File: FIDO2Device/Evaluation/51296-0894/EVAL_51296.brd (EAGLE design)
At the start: 25 x 30 mm, 14 parts, among them CN1 51296-0894, CN2 IF_6PIN, CN3 IF_4PIN, Q1 BSS84AKQBZ, U1 RV-3028-C7

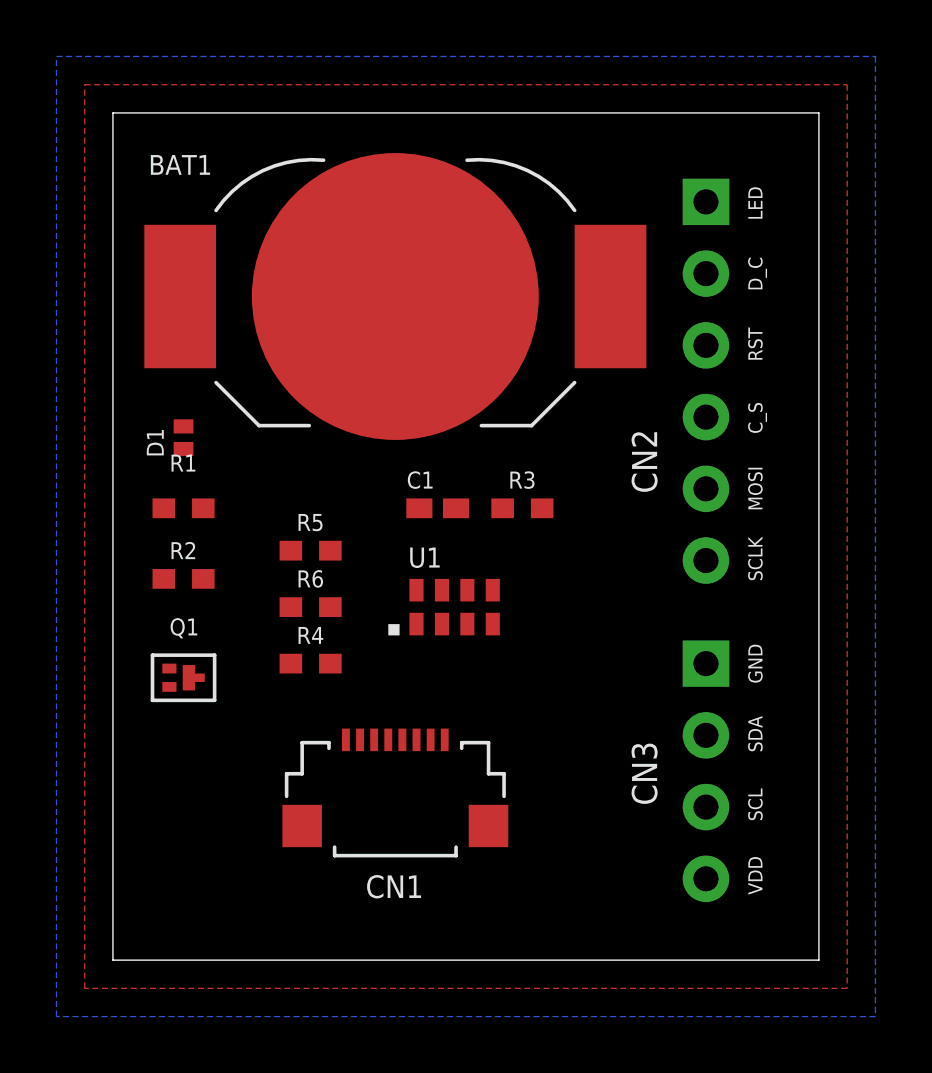
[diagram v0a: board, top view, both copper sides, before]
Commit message: 配線レイアウトを作成
・部品の配置を変更
（RTCC回路を基板の右下部に寄せる）
・電源ライン用のviaを配置
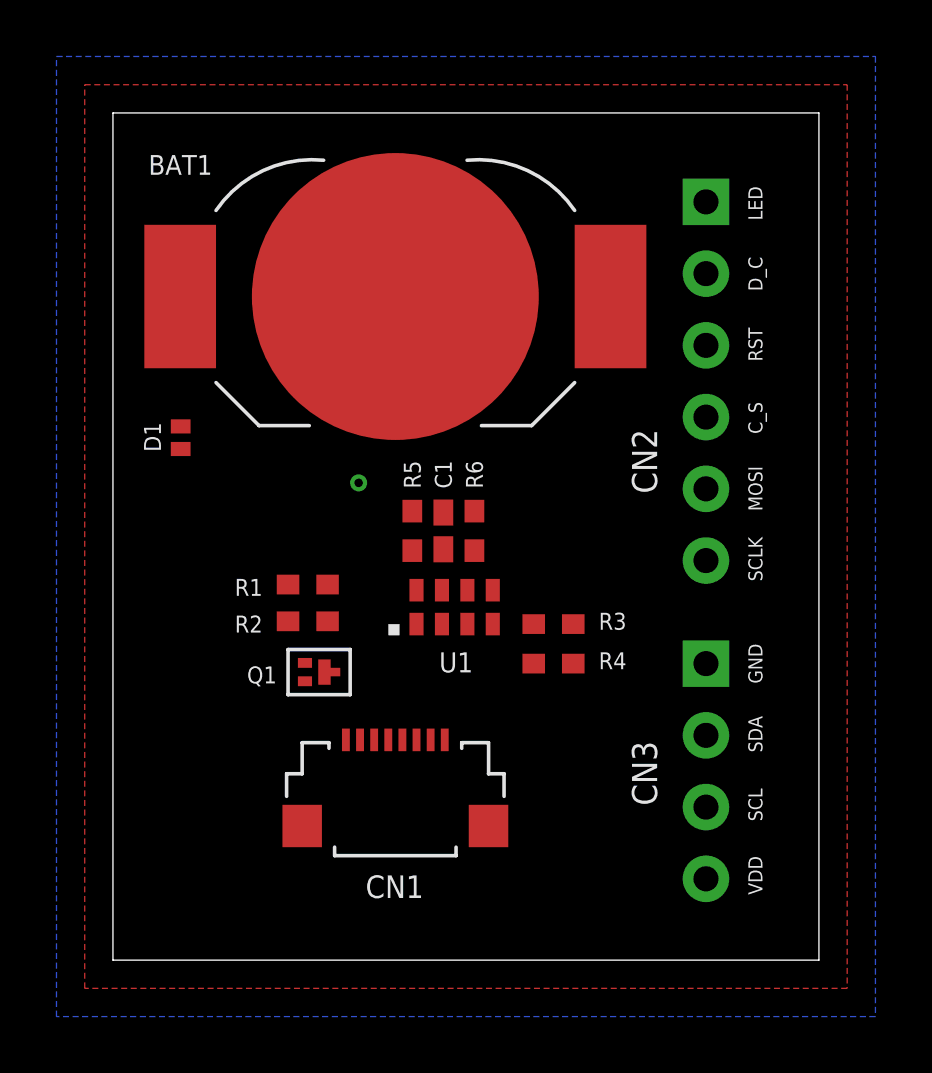
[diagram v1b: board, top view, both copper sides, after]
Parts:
- moved R4 8.60 mm to (15.6, 10.5)
- moved R6 6.40 mm to (12.8, 15.2), turned to 270 degrees
- moved R1 5.16 mm to (6.90, 13.3)
- moved Q1 4.80 mm to (7.30, 10.2)
- moved R2 4.65 mm to (6.90, 12.0)
- moved R3 4.24 mm to (15.6, 11.9)
- moved R5 3.67 mm to (10.6, 15.2), turned to 270 degrees
- moved C1 0.82 mm to (11.7, 15.2), turned to 90 degrees
- moved D1 0.10 mm to (2.40, 18.5)
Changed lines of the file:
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@@
 <attribute name="VALUE" x="19.73" y="11.77" size="0.889" layer="27" ratio="11" rot="R270" align="top-left"/>
 </element>
-<element name="Q1" library="Parts" package="BSS84AKQB" value="BSS84AKQBZ" x="2.5" y="10" smashed="yes" rot="R90">
-<attribute name="NAME" x="2" y="11.5" size="0.6" layer="25"/>
-<attribute name="VALUE" x="2.5" y="11" size="0.6" layer="27" rot="R90"/>
+<element name="Q1" library="Parts" package="BSS84AKQB" value="BSS84AKQBZ" x="7.3" y="10.2" smashed="yes" rot="R90">
+<attribute name="NAME" x="5.8" y="10.4" size="0.6" layer="25" rot="R180"/>
+<attribute name="VALUE" x="7.3" y="11.2" size="0.6" layer="27" rot="R90"/>
 </element>
 <element name="BAT1" library="Connectors" package="BAT-HLD-012-SMT" value="BAT-HLD-012-SMT" x="10" y="23.5" smashed="yes" rot="R180">
@@
 <attribute name="VALUE" x="0.17" y="22.71" size="0.7" layer="27" rot="R180"/>
 </element>
-<element name="R1" library="Parts" package="R0402N" value="5.1k" x="2.5" y="16" smashed="yes" rot="R180">
-<attribute name="NAME" x="2" y="17.3" size="0.6" layer="25"/>
-<attribute name="VALUE" x="3" y="17.3" size="0.6" layer="27" rot="R180"/>
+<element name="R1" library="Parts" package="R0402N" value="5.1k" x="6.9" y="13.3" smashed="yes" rot="R180">
+<attribute name="NAME" x="5.3" y="13.5" size="0.6" layer="25" rot="R180"/>
+<attribute name="VALUE" x="7.4" y="14.6" size="0.6" layer="27" rot="R180"/>
 </element>
-<element name="R2" library="Parts" package="R0402N" value="20k" x="2.5" y="13.5" smashed="yes">
-<attribute name="NAME" x="2" y="14.2" size="0.6" layer="25"/>
-<attribute name="VALUE" x="2" y="12.2" size="0.6" layer="27"/>
+<element name="R2" library="Parts" package="R0402N" value="20k" x="6.9" y="12" smashed="yes">
+<attribute name="NAME" x="5.3" y="12.2" size="0.6" layer="25" rot="R180"/>
+<attribute name="VALUE" x="6.4" y="10.7" size="0.6" layer="27"/>
 </element>
-<element name="U1" library="ICs" package="SON-8" value="RV-3028-C7" x="10.5" y="11.5"/>
-<element name="R3" library="Parts" package="R0402N" value="10k" x="14.5" y="16"/>
-<element name="R4" library="Parts" package="R0402N" value="10k" x="7" y="10.5"/>
-<element name="R5" library="Parts" package="R0402N" value="10k" x="7" y="14.5" smashed="yes">
-<attribute name="NAME" x="6.5" y="15.2" size="0.6" layer="25"/>
-<attribute name="VALUE" x="6.5" y="13.2" size="0.6" layer="27"/>
+<element name="U1" library="ICs" package="SON-8" value="RV-3028-C7" x="10.5" y="11.5" smashed="yes">
+<attribute name="NAME" x="12.75" y="10.9" size="0.7112" layer="25" rot="R180"/>
+<attribute name="VALUE" x="10.45" y="10.4" size="0.7112" layer="27"/>
 </element>
-<element name="C1" library="Parts" package="C0402N" value="0.1uF" x="11.5" y="16"/>
-<element name="R6" library="Parts" package="R0402N" value="10k" x="7" y="12.5"/>
-<element name="D1" library="Parts" package="DFN1006D-2" value="PMEG2005BELD,315" x="2.5" y="18.5" rot="R90"/>
+<element name="R3" library="Parts" package="R0402N" value="10k" x="15.6" y="11.9" smashed="yes">
+<attribute name="NAME" x="17.2" y="11.7" size="0.6" layer="25"/>
+<attribute name="VALUE" x="15.1" y="10.6" size="0.6" layer="27"/>
+</element>
+<element name="R4" library="Parts" package="R0402N" value="10k" x="15.6" y="10.5" smashed="yes">
+<attribute name="NAME" x="17.2" y="10.3" size="0.6" layer="25"/>
+<attribute name="VALUE" x="15.1" y="9.2" size="0.6" layer="27"/>
+</element>
+<element name="R5" library="Parts" package="R0402N" value="10k" x="10.6" y="15.2" smashed="yes" rot="R270">
+<attribute name="NAME" x="10.9" y="16.7" size="0.6" layer="25" rot="R90"/>
+<attribute name="VALUE" x="9.3" y="15.7" size="0.6" layer="27" rot="R270"/>
+</element>
+<element name="C1" library="Parts" package="C0402N" value="0.1uF" x="11.7" y="15.2" smashed="yes" rot="R90">
+<attribute name="NAME" x="12" y="16.7" size="0.6" layer="25" rot="R90"/>
+<attribute name="VALUE" x="13" y="14.1" size="0.6" layer="27" rot="R90"/>
+</element>
+<element name="R6" library="Parts" package="R0402N" value="10k" x="12.8" y="15.2" smashed="yes" rot="R270">
+<attribute name="NAME" x="13.1" y="16.7" size="0.6" layer="25" rot="R90"/>
+<attribute name="VALUE" x="11.5" y="15.7" size="0.6" layer="27" rot="R270"/>
+</element>
+<element name="D1" library="Parts" package="DFN1006D-2" value="PMEG2005BELD,315" x="2.4" y="18.5" smashed="yes" rot="R90">
+<attribute name="NAME" x="1.7" y="18" size="0.6" layer="25" rot="R90"/>
+<attribute name="VALUE" x="3.1" y="17.8" size="0.6" layer="27" rot="R90" align="top-left"/>
+</element>
 </elements>
 <signals>
@@
 <contactref element="CN1" pad="1"/>
 <contactref element="Q1" pad="3"/>
-<wire x1="2.69" y1="10" x2="8.25" y2="7.8" width="0" layer="19" extent="1-1"/>
+<wire x1="7.49" y1="10.2" x2="8.25" y2="7.8" width="0" layer="19" extent="1-1"/>
 </signal>
 <signal name="0V">
@@
 <contactref element="Q1" pad="1"/>
 <contactref element="R2" pad="1"/>
-<wire x1="1.8" y1="13.5" x2="1.8" y2="16" width="0" layer="19" extent="1-1"/>
-<wire x1="2" y1="9.675" x2="1.8" y2="13.5" width="0" layer="19" extent="1-1"/>
+<wire x1="6.2" y1="12" x2="6.2" y2="13.3" width="0" layer="19" extent="1-1"/>
+<wire x1="6.8" y1="9.875" x2="6.2" y2="12" width="0" layer="19" extent="1-1"/>
 </signal>
 <signal name="VDD_NRF">
@@
 <contactref element="R4" pad="2"/>
 <contactref element="D1" pad="1"/>
-<wire x1="15.2" y1="16" x2="21" y2="2.88" width="0" layer="19" extent="1-1"/>
-<wire x1="10.85" y1="16" x2="15.2" y2="16" width="0" layer="19" extent="1-1"/>
-<wire x1="11.65" y1="13.1" x2="10.85" y2="16" width="0" layer="19" extent="1-1"/>
-<wire x1="7.7" y1="10.5" x2="11.65" y2="13.1" width="0" layer="19" extent="1-1"/>
-<wire x1="3.2" y1="13.5" x2="7.7" y2="10.5" width="0" layer="19" extent="1-1"/>
-<wire x1="2" y1="10.325" x2="3.2" y2="13.5" width="0" layer="19" extent="1-1"/>
-<wire x1="11.25" y1="7.8" x2="11.65" y2="13.1" width="0" layer="19" extent="1-1"/>
-<wire x1="2.5" y1="18.1" x2="3.2" y2="13.5" width="0" layer="19" extent="1-1"/>
+<wire x1="16.3" y1="10.5" x2="16.3" y2="11.9" width="0" layer="19" extent="1-1"/>
+<wire x1="11.65" y1="13.1" x2="16.3" y2="11.9" width="0" layer="19" extent="1-1"/>
+<wire x1="11.7" y1="14.55" x2="11.65" y2="13.1" width="0" layer="19" extent="1-1"/>
+<wire x1="7.6" y1="12" x2="11.65" y2="13.1" width="0" layer="19" extent="1-1"/>
+<wire x1="6.8" y1="10.525" x2="7.6" y2="12" width="0" layer="19" extent="1-1"/>
+<wire x1="11.25" y1="7.8" x2="6.8" y2="10.525" width="0" layer="19" extent="1-1"/>
+<wire x1="2.4" y1="18.1" x2="7.6" y2="12" width="0" layer="19" extent="1-1"/>
+<wire x1="21" y1="2.88" x2="16.3" y2="10.5" width="0" layer="19" extent="1-1"/>
 </signal>
 <signal name="LED_CTRL">
 <contactref element="R1" pad="1"/>
 <contactref element="CN2" pad="1"/>
-<wire x1="3.2" y1="16" x2="21" y2="26.85" width="0" layer="19" extent="1-1"/>
+<wire x1="7.6" y1="13.3" x2="21" y2="26.85" width="0" layer="19" extent="1-1"/>
 </signal>
 <signal name="CS">
@@
 <contactref element="R3" pad="1"/>
 <contactref element="CN3" pad="2"/>
-<wire x1="13.8" y1="16" x2="21" y2="7.96" width="0" layer="19" extent="1-1"/>
-<wire x1="13.45" y1="11.9" x2="13.8" y2="16" width="0" layer="19" extent="1-1"/>
+<wire x1="14.9" y1="11.9" x2="21" y2="7.96" width="0" layer="19" extent="1-1"/>
+<wire x1="13.45" y1="11.9" x2="14.9" y2="11.9" width="0" layer="19" extent="1-1"/>
 </signal>
 <signal name="TWI_SCL">
@@
 <contactref element="R4" pad="1"/>
 <contactref element="CN3" pad="3"/>
-<wire x1="12.55" y1="11.9" x2="21" y2="5.42" width="0" layer="19" extent="1-1"/>
-<wire x1="6.3" y1="10.5" x2="12.55" y2="11.9" width="0" layer="19" extent="1-1"/>
+<wire x1="14.9" y1="10.5" x2="21" y2="5.42" width="0" layer="19" extent="1-1"/>
+<wire x1="12.55" y1="11.9" x2="14.9" y2="10.5" width="0" layer="19" extent="1-1"/>
 </signal>
 <signal name="N$9">
 <contactref element="U1" pad="6"/>
 <contactref element="R6" pad="2"/>
-<wire x1="7.7" y1="12.5" x2="12.55" y2="13.1" width="0" layer="19" extent="1-1"/>
+<wire x1="12.55" y1="13.1" x2="12.8" y2="14.5" width="0" layer="19" extent="1-1"/>
 </signal>
 <signal name="N$10">
 <contactref element="U1" pad="8"/>
 <contactref element="R5" pad="2"/>
-<wire x1="10.75" y1="13.1" x2="7.7" y2="14.5" width="0" layer="19" extent="1-1"/>
+<wire x1="10.6" y1="14.5" x2="10.75" y2="13.1" width="0" layer="19" extent="1-1"/>
 </signal>
 <signal name="N$2">
 <contactref element="BAT1" pad="+@2"/>
 <contactref element="D1" pad="2"/>
-<wire x1="2.5" y1="18.9" x2="2.38" y2="23.5" width="0" layer="19" extent="1-1"/>
+<wire x1="2.4" y1="18.9" x2="2.38" y2="23.5" width="0" layer="19" extent="1-1"/>
+</signal>
+<signal name="N$3">
+<via x="8.7" y="16.9" extent="1-16" drill="0.3"/>
 </signal>
 </signals>

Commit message: 配線レイアウトを作成
・電源ラインの配線
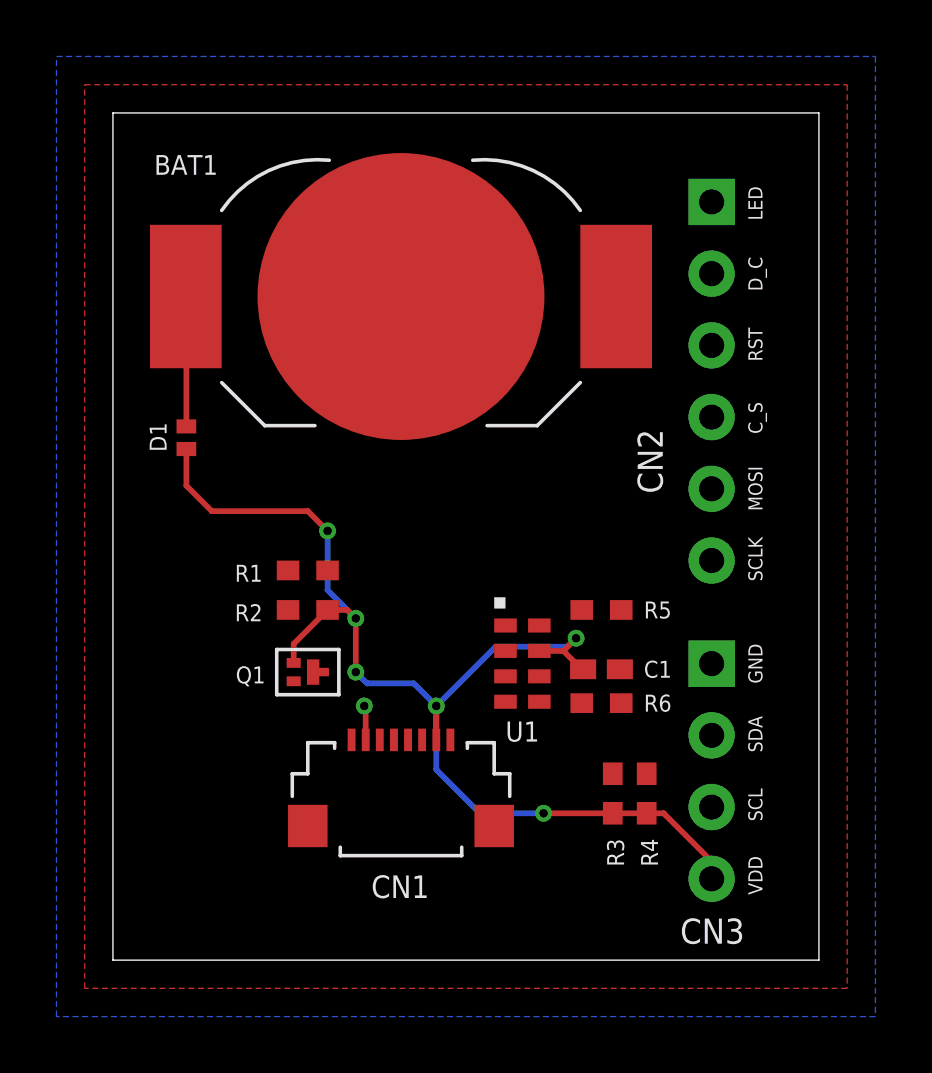
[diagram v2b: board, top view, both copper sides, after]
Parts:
- moved R6 7.58 mm to (17.3, 9.10), turned to 180 degrees
- moved C1 7.44 mm to (17.3, 10.3), turned to 0 degrees
- moved R5 7.26 mm to (17.3, 12.4), turned to 180 degrees
- moved R3 6.36 mm to (17.7, 5.90), turned to 270 degrees
- moved R4 5.66 mm to (18.9, 5.90), turned to 270 degrees
- moved U1 3.06 mm to (13.5, 12.1), turned to 270 degrees
- moved R1 0.50 mm to (6.90, 13.8)
- moved R2 0.40 mm to (6.90, 12.4)
- moved Q1 0.40 mm to (6.90, 10.2)
- moved D1 0.20 mm to (2.60, 18.5)
- moved BAT1 0.20 mm to (10.2, 23.5)
- moved CN1 0.20 mm to (10.2, 4.00)
- moved CN2 0.20 mm to (21.2, 20.5)
- moved CN3 0.20 mm to (21.2, 10.5)
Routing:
- net VDD_NRF: track 0.00 -> 43.0 mm, vias 0 -> 6
- net N$2: track 0.00 -> 4.61 mm
- net 0V: track 0.00 -> 1.22 mm, vias 0 -> 1

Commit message: 配線レイアウトを作成
・LED制御回路、RTCC回路の配線
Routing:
- net LED_CTRL: track 0.00 -> 22.0 mm
- net TWI_SCL: track 0.00 -> 12.7 mm
- net TWI_SDA: track 0.00 -> 9.94 mm
- net N$1: track 0.00 -> 5.18 mm
- net LEDA: track 0.00 -> 3.20 mm
- net N$9: track 0.00 -> 1.89 mm
- net N$10: track 0.00 -> 1.73 mm
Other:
- board text added: "RTCC"
- board text added: "TFT Module"
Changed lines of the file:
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@@
 <dimension x1="0" y1="0" x2="0" y2="30" x3="-3" y3="15" textsize="1.778" layer="51"/>
 <dimension x1="0" y1="30" x2="25" y2="30" x3="12.5" y3="33" textsize="1.778" layer="51"/>
+<text x="23.4" y="20.5" size="0.7" layer="21" rot="R90" align="top-center">TFT Module</text>
+<text x="23.4" y="6.7" size="0.7" layer="21" rot="R90" align="top-center">RTCC</text>
 </plain>
 <attributes>
@@
 </element>
 <element name="CN2" library="Connectors" package="HEADER_6PIN" value="IF_6PIN" x="21.2" y="20.5" smashed="yes" rot="R270">
-<attribute name="NAME" x="19.47" y="16.52" size="0.889" layer="25" ratio="11" rot="R90"/>
+<attribute name="NAME" x="19.97" y="28.32" size="0.889" layer="25" ratio="11"/>
 <attribute name="VALUE" x="19.93" y="28.12" size="0.889" layer="27" ratio="11" rot="R270" align="top-left"/>
 </element>
@@
 <contactref element="CN1" pad="1"/>
 <contactref element="Q1" pad="3"/>
-<wire x1="7.09" y1="10.2" x2="8.45" y2="7.8" width="0" layer="19" extent="1-1"/>
+<wire x1="8.45" y1="7.8" x2="8.45" y2="8.45" width="0.2032" layer="1"/>
+<wire x1="8.45" y1="8.45" x2="7.9" y2="9" width="0.2032" layer="1"/>
+<wire x1="7.9" y1="9" x2="7.5" y2="9" width="0.2032" layer="1"/>
+<wire x1="7.09" y1="10.2" x2="7.09" y2="9.41" width="0.2032" layer="1"/>
+<wire x1="7.09" y1="9.41" x2="7.5" y2="9" width="0.2032" layer="1"/>
 </signal>
 <signal name="0V">
@@
 <vertex x="-2" y="-2"/>
 </polygon>
-<via x="8.9" y="9" extent="1-16" drill="0.3"/>
-<wire x1="8.95" y1="7.8" x2="8.95" y2="8.95" width="0.2032" layer="1"/>
-<wire x1="8.95" y1="8.95" x2="8.9" y2="9" width="0.2032" layer="1"/>
+<via x="8.9" y="6.6" extent="1-16" drill="0.3"/>
+<wire x1="8.95" y1="7.8" x2="8.95" y2="6.65" width="0.2032" layer="1"/>
+<wire x1="8.95" y1="6.65" x2="8.9" y2="6.6" width="0.2032" layer="1"/>
 </signal>
 <signal name="N$1">
@@
 <contactref element="Q1" pad="1"/>
 <contactref element="R2" pad="1"/>
-<wire x1="6.2" y1="12.4" x2="6.2" y2="13.8" width="0" layer="19" extent="1-1"/>
-<wire x1="6.4" y1="9.875" x2="6.2" y2="12.4" width="0" layer="19" extent="1-1"/>
+<wire x1="6.2" y1="13.8" x2="6.2" y2="12.4" width="0.2032" layer="1"/>
+<wire x1="6.4" y1="9.875" x2="5.925" y2="9.875" width="0.2032" layer="1"/>
+<wire x1="5.925" y1="9.875" x2="5.4" y2="10.4" width="0.2032" layer="1"/>
+<wire x1="5.4" y1="10.4" x2="5.4" y2="12" width="0.2032" layer="1"/>
+<wire x1="6.2" y1="12.4" x2="5.8" y2="12.4" width="0.2032" layer="1"/>
+<wire x1="5.8" y1="12.4" x2="5.4" y2="12" width="0.2032" layer="1"/>
 </signal>
 <signal name="VDD_NRF">
@@
 <contactref element="R1" pad="1"/>
 <contactref element="CN2" pad="1"/>
-<wire x1="7.6" y1="13.8" x2="21.2" y2="26.85" width="0" layer="19" extent="1-1"/>
+<wire x1="7.6" y1="13.8" x2="7.6" y2="14.4" width="0.2032" layer="1"/>
+<wire x1="7.6" y1="14.4" x2="10.1" y2="16.9" width="0.2032" layer="1"/>
+<wire x1="10.1" y1="16.9" x2="13" y2="16.9" width="0.2032" layer="1"/>
+<wire x1="21.2" y1="26.85" x2="19.7" y2="25.35" width="0.2032" layer="1"/>
+<wire x1="19.7" y1="25.35" x2="19.7" y2="20.8" width="0.2032" layer="1"/>
+<wire x1="13" y1="16.9" x2="16.4" y2="20.3" width="0.2032" layer="1"/>
+<wire x1="16.4" y1="20.3" x2="19.2" y2="20.3" width="0.2032" layer="1"/>
+<wire x1="19.2" y1="20.3" x2="19.7" y2="20.8" width="0.2032" layer="1"/>
 </signal>
 <signal name="CS">
@@
 <contactref element="R3" pad="1"/>
 <contactref element="CN3" pad="2"/>
-<wire x1="17.7" y1="6.6" x2="21.2" y2="7.96" width="0" layer="19" extent="1-1"/>
-<wire x1="13.9" y1="9.15" x2="17.7" y2="6.6" width="0" layer="19" extent="1-1"/>
+<wire x1="17.7" y1="6.6" x2="14.7" y2="6.6" width="0.2032" layer="1"/>
+<wire x1="13.9" y1="9.15" x2="13.9" y2="7.4" width="0.2032" layer="1"/>
+<wire x1="13.9" y1="7.4" x2="14.7" y2="6.6" width="0.2032" layer="1"/>
+<wire x1="21.2" y1="7.96" x2="20.74" y2="7.5" width="0.2032" layer="1"/>
+<wire x1="20.74" y1="7.5" x2="18.6" y2="7.5" width="0.2032" layer="1"/>
+<wire x1="17.7" y1="6.6" x2="18.6" y2="7.5" width="0.2032" layer="1"/>
 </signal>
 <signal name="TWI_SCL">
@@
 <contactref element="R4" pad="1"/>
 <contactref element="CN3" pad="3"/>
-<wire x1="18.9" y1="6.6" x2="21.2" y2="5.42" width="0" layer="19" extent="1-1"/>
-<wire x1="13.9" y1="10.05" x2="18.9" y2="6.6" width="0" layer="19" extent="1-1"/>
+<wire x1="18.9" y1="6.6" x2="18.2" y2="5.9" width="0.2032" layer="1"/>
+<wire x1="14.7" y1="5.9" x2="13.1" y2="7.5" width="0.2032" layer="1"/>
+<wire x1="13.1" y1="7.5" x2="13.1" y2="9.7" width="0.2032" layer="1"/>
+<wire x1="18.9" y1="6.6" x2="20.02" y2="6.6" width="0.2032" layer="1"/>
+<wire x1="20.02" y1="6.6" x2="21.2" y2="5.42" width="0.2032" layer="1"/>
+<wire x1="18.2" y1="5.9" x2="14.7" y2="5.9" width="0.2032" layer="1"/>
+<wire x1="13.9" y1="10.05" x2="13.45" y2="10.05" width="0.2032" layer="1"/>
+<wire x1="13.1" y1="9.7" x2="13.45" y2="10.05" width="0.2032" layer="1"/>
 </signal>
 <signal name="N$9">
 <contactref element="U1" pad="6"/>
 <contactref element="R6" pad="2"/>
-<wire x1="15.1" y1="10.05" x2="16.6" y2="9.1" width="0" layer="19" extent="1-1"/>
+<wire x1="16.6" y1="9.1" x2="15.65" y2="10.05" width="0.2032" layer="1"/>
+<wire x1="15.65" y1="10.05" x2="15.1" y2="10.05" width="0.2032" layer="1"/>
 </signal>
 <signal name="N$10">
 <contactref element="U1" pad="8"/>
 <contactref element="R5" pad="2"/>
-<wire x1="15.1" y1="11.85" x2="16.6" y2="12.4" width="0" layer="19" extent="1-1"/>
+<wire x1="16.6" y1="12.4" x2="16.05" y2="11.85" width="0.2032" layer="1"/>
+<wire x1="16.05" y1="11.85" x2="15.1" y2="11.85" width="0.2032" layer="1"/>
 </signal>
 <signal name="N$2">
